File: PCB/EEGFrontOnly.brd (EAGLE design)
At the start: 87.5 x 46.7 mm, 107 parts, among them IC1 ADS1299-X, IC2 ADUM3151-3, U1 LP2985-33DBVT, U10 ISO721D, U2 B0505S-1WB0505S-1W, U3 TPS60403DBVT, U4 TPS73225DBVR, U5 TPS73225DBVR, U6 TPD4E1B06DCKR, U7 TPD4E1B06DCKR, U8 TPD4E1B06DCKR, U9 HT7333

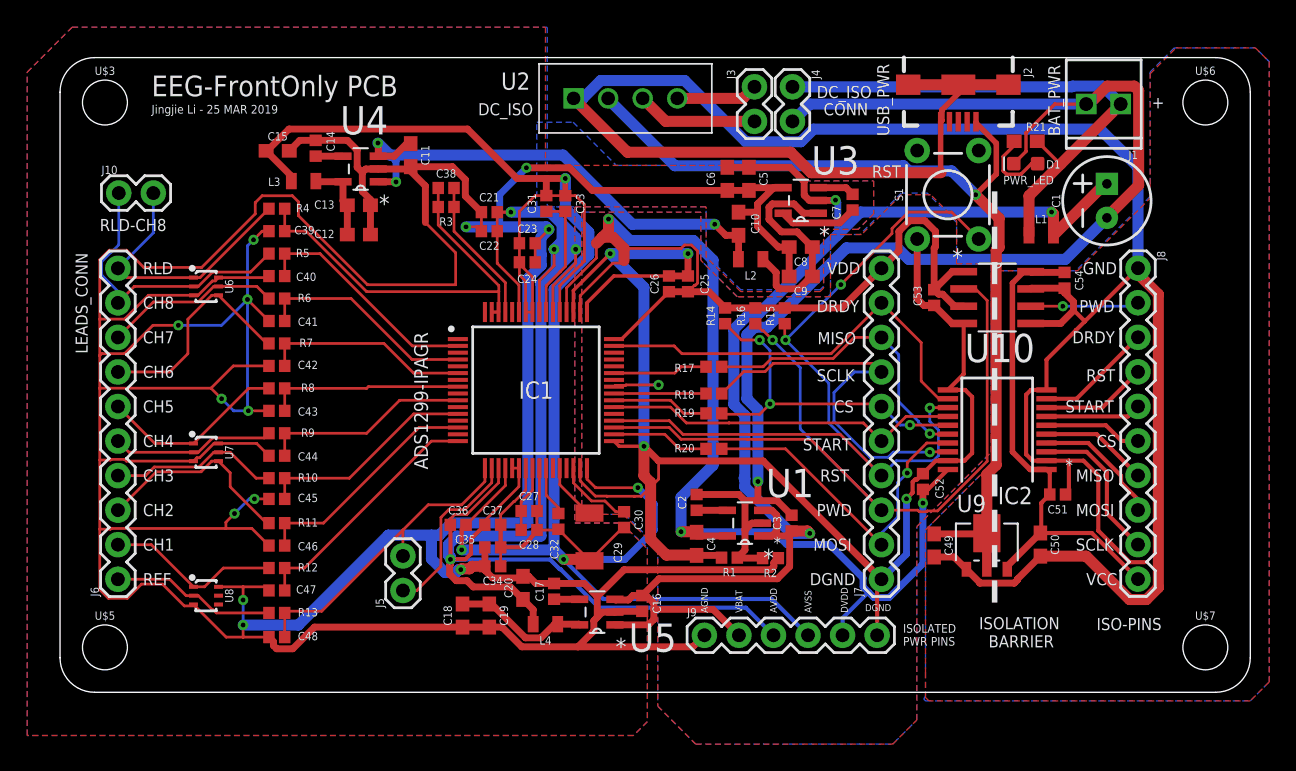
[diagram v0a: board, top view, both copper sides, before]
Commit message: update EEG ADS PCB
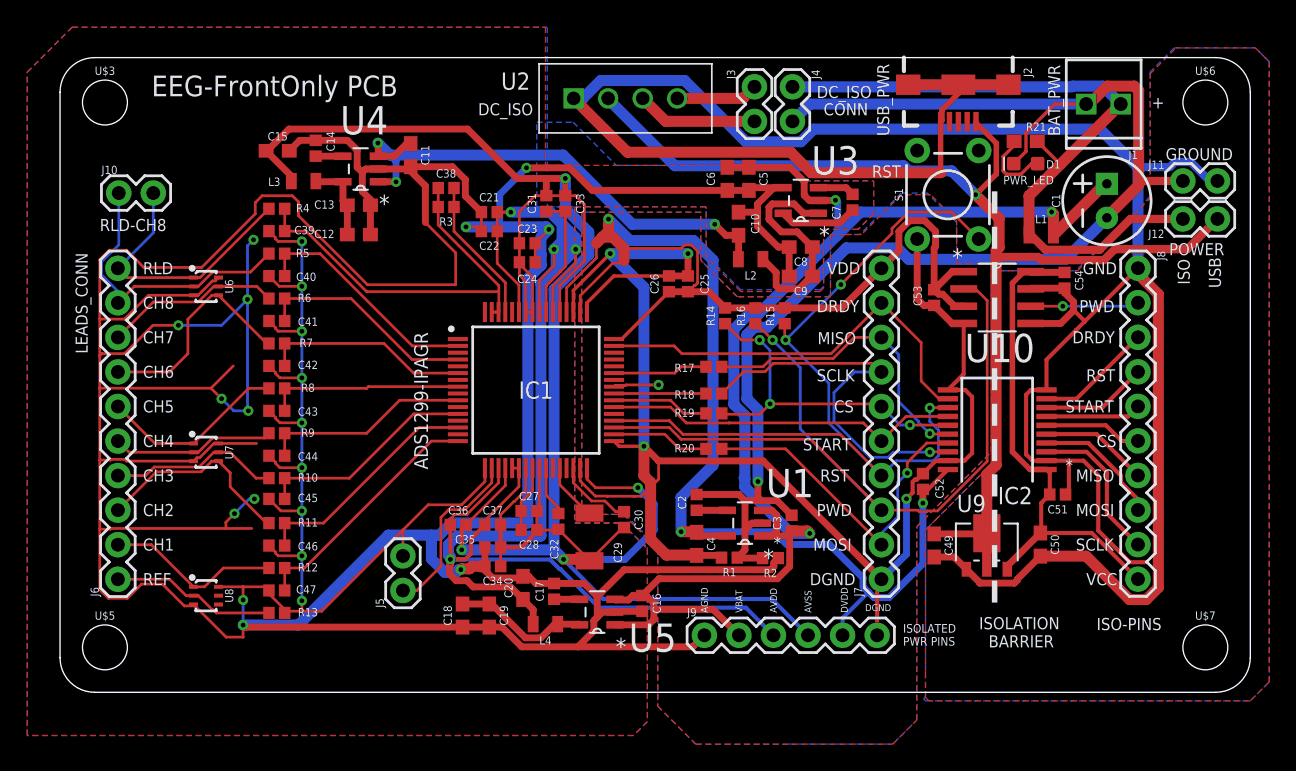
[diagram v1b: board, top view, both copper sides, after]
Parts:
- removed C48: 4.7nF, SparkFun-Capacitors:0402
- added J11, J12: (no value), SparkFun-Connectors:1X02
- C39: value 4.7nF -> NI
- R4: value 4.99K -> 0OHM
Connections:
- net AGND: no longer C39.2, C40.2, C41.2, C42.2, C43.2, C44.2, C45.2, C46.2, C47.2, C48.2
- net GND: now also J11.1
- net GND-ISO: now also J11.2
- net N$12: now also C39.2, C40.2, C41.2, C42.2, C43.2, C44.2, C45.2, C46.2, C47.2; no longer C48.1
- net VBATPRE: now also J12.1
- net VCC-ISO: now also J12.2
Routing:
- net N$12: track 23.4 -> 73.2 mm, vias 0 -> 9
- net VCC-ISO: track 68.8 -> 86.4 mm
- net AGND: track 371.3 -> 354.2 mm
- net VBATPRE: track 39.6 -> 52.3 mm
- net GND-ISO: track 184.4 -> 191.0 mm
- net GND: track 103.6 -> 107.0 mm
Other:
- board text added: "GROUND"
- board text added: "ISO"
- board text added: "POWER"
- board text added: "USB"
- board text removed: "Jingjie Li - 25 MAR 2019"
